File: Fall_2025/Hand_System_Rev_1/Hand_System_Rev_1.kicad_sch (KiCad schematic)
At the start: 33 parts, among them J1 Barrel_Jack, M1 Motor_Servo, M2 Motor_Servo, M3 Motor_Servo, M4 Motor_Servo, M5 Motor_Servo, M6 Motor_Servo, M7 Stepper_Motor, U1 ESP32-DEVKITC-32UE, U2 LM2596, U3 A4988_Stepper_Motor_Driver, U5 MAX9814ETD_T

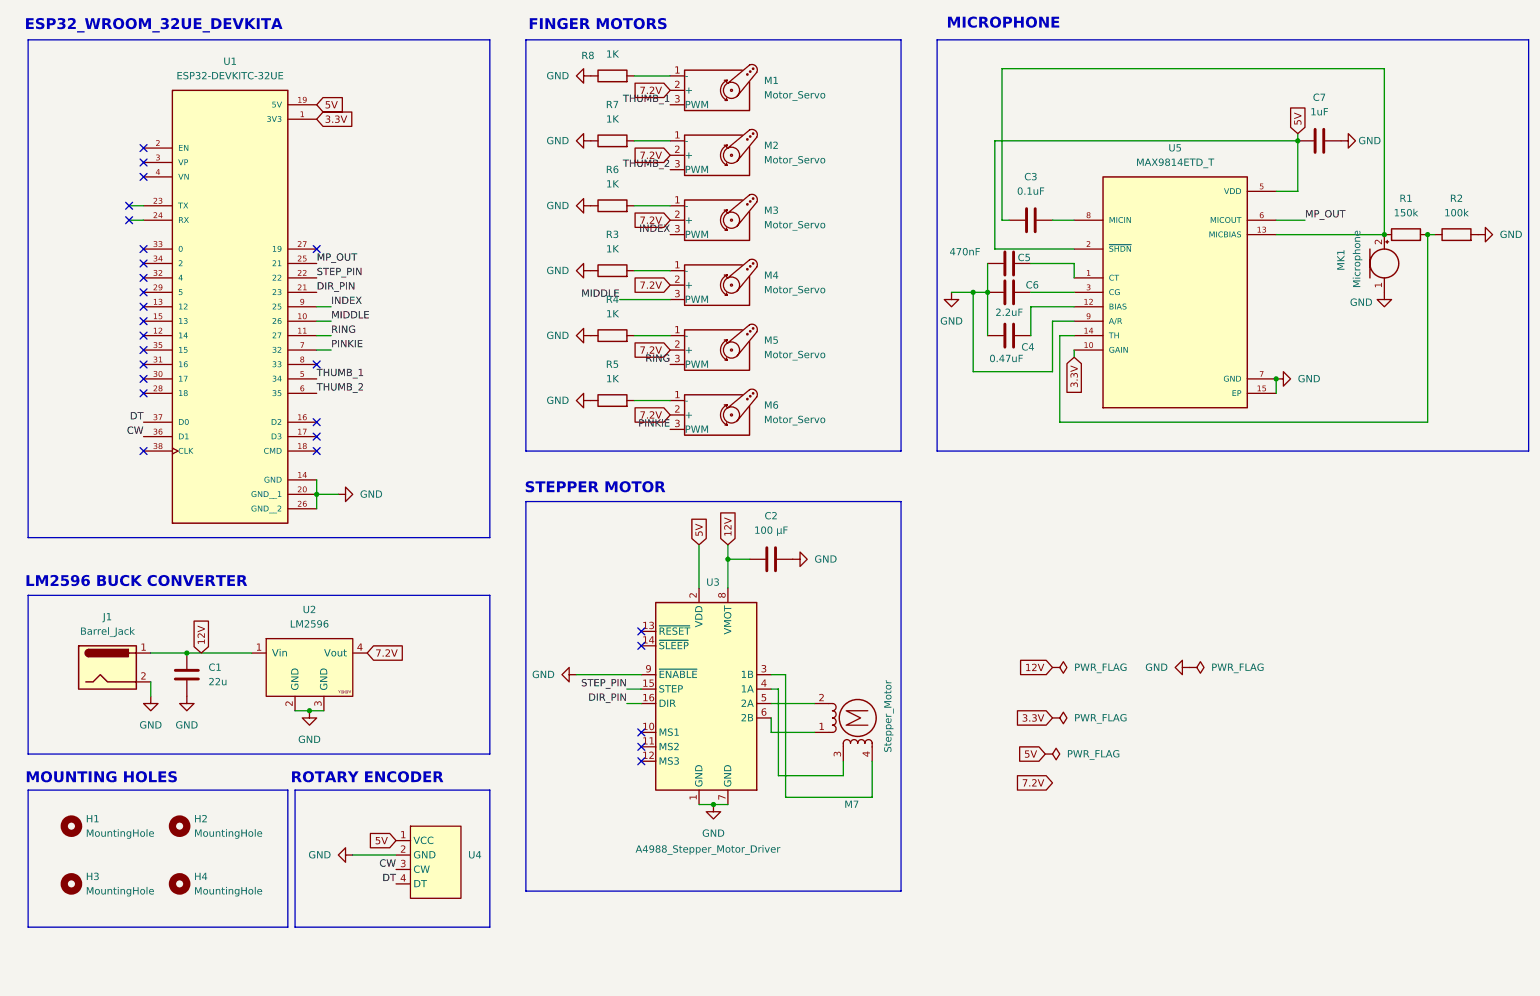
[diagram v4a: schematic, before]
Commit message: update electrical schematic to include 10 servo motors, two buck converteds, and removed microphone
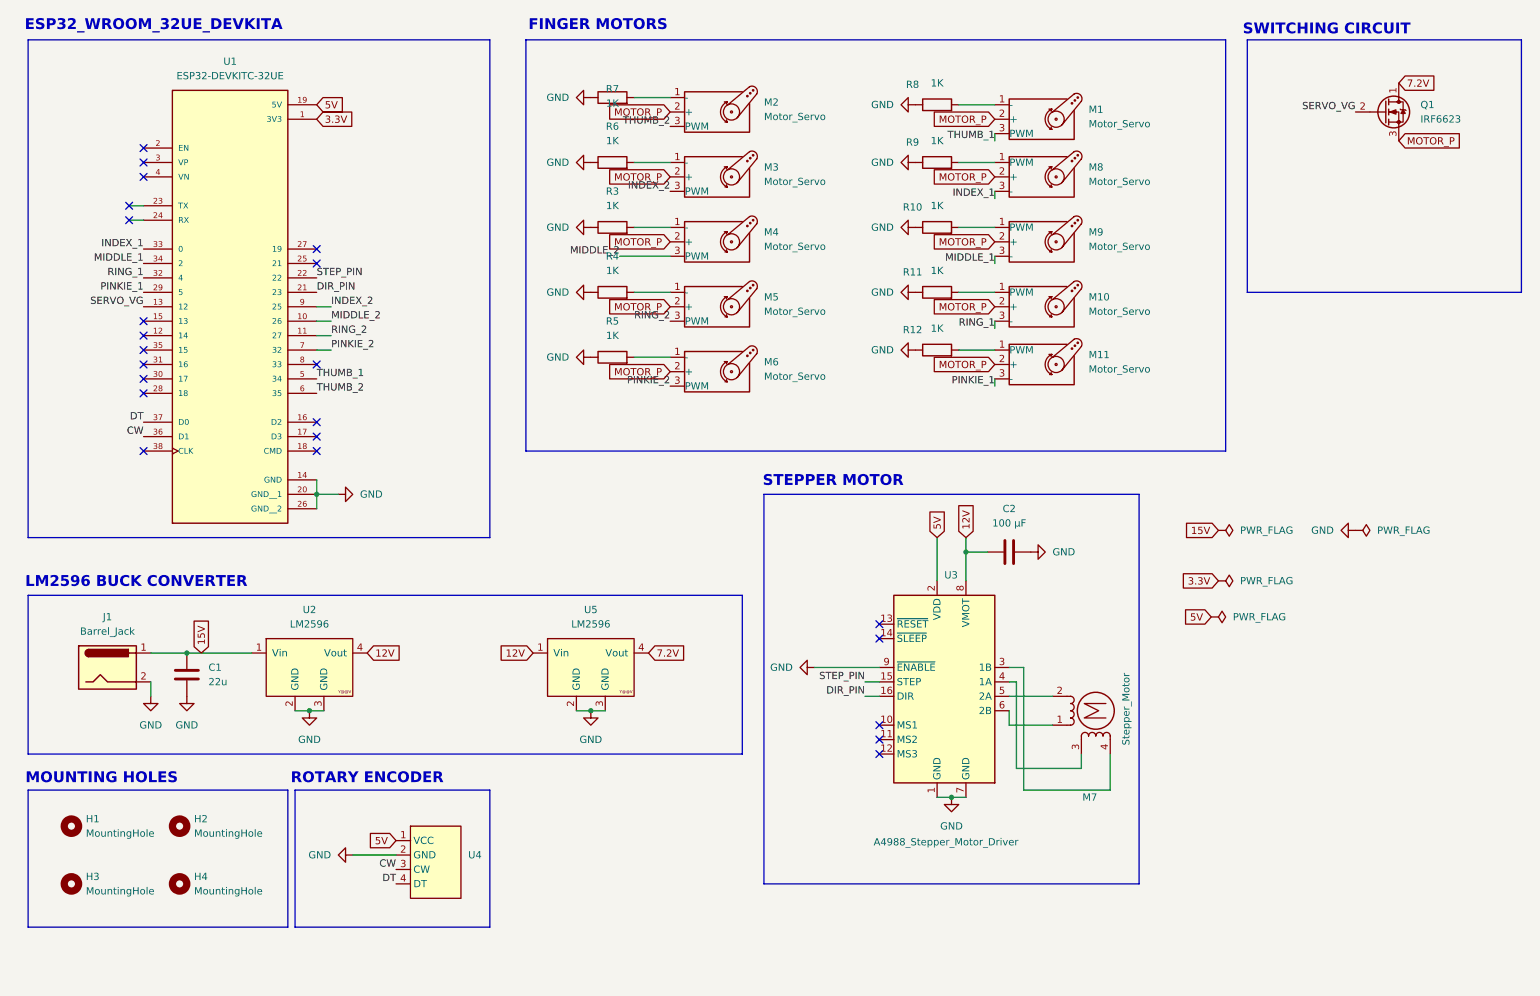
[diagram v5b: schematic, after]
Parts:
- removed C3: 0.1uF, Capacitor_SMD:C_0805_2012Metric, symbol Device:C
- removed C4: 0.47uF, Capacitor_SMD:C_0805_2012Metric, symbol Device:C
- removed C5: 470nF, Capacitor_SMD:C_0805_2012Metric, symbol Device:C
- removed C6: 2.2uF, Capacitor_SMD:C_0805_2012Metric, symbol Device:C
- removed C7: 1uF, Capacitor_SMD:C_0805_2012Metric, symbol Device:C
- removed MK1: Microphone, Sensor_Audio:POM-2244P-C3310-2-R, symbol Device:Microphone
- removed R1: 150k, Resistor_SMD:R_0805_2012Metric, symbol Device:R
- removed R2: 100k, Resistor_SMD:R_0805_2012Metric, symbol Device:R
- removed U5: MAX9814ETD_T, MAX9814ETD_T:SON40P300X300X80-15N, symbol MAX9814ETD_T:MAX9814ETD_T
- added M10, M11, M8, M9: Motor_Servo, symbol Motor:Motor_Servo
- added Q1: IRF6623, Package_DirectFET:DirectFET_ST, symbol Transistor_FET:IRF6623
- added R10, R11, R12, R9: 1K, Resistor_SMD:R_0805_2012Metric, symbol Device:R
- added U5: LM2596, PCB_Components:LM2596, symbol Schematic:LM2596
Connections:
- net 12V: now also U2.4 (Vout), U5.1 (Vin); no longer C1.1, J1.1, U2.1 (Vin)
- net 7.2V: now also Q1.1 (D), U5.4 (Vout); no longer M1.2 (+), M2.2 (+), M3.2 (+), M4.2 (+), M5.2 (+), M6.2 (+), U2.4 (Vout)
- net GND: now also R10.1, R11.1, R12.1, R9.1, U5.2 (GND), U5.3 (GND)
- net SERVO_VG: now reaches U1.13 (12)
- net SERVO_VG: now also Q1.2 (G)
- net PINKIE_1: now reaches U1.29 (5)
- net PINKIE_1: now also M11.3 (-)
- net RING_1: now reaches U1.32 (4)
- net RING_1: now also M10.3 (-)
- net INDEX_1: now reaches U1.33 (0)
- net INDEX_1: now also M8.3 (-)
- net MIDDLE_1: now reaches U1.34 (2)
- net MIDDLE_1: now also M9.3 (-)
- net INDEX renamed INDEX_2
- net MIDDLE renamed MIDDLE_2
- net MP_OUT: no longer names the net of U1.25 (21)
- net PINKIE renamed PINKIE_2
- net RING renamed RING_2
- new net: M8.1 (PWM), R9.2
- new net: M10.1 (PWM), R11.2
- new net: M11.1 (PWM), R12.2
- new net: M9.1 (PWM), R10.2
- new net 15V: C1.1, J1.1, U2.1 (Vin)
- new net MOTOR_P: M1.2 (+), M10.2 (+), M11.2 (+), M2.2 (+), M3.2 (+), M4.2 (+), M5.2 (+), M6.2 (+), M8.2 (+), M9.2 (+), Q1.3 (S)
- no-connect marks 27 -> 23
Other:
- note added: "SWITCHING CIRCUIT"
- note removed: "MICROPHONE"
- moved on the sheet: C2, M1, M2, M3, M4, M5, M6, M7, R3, R4, R5, R6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

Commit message: added more stuff for switching circuitry
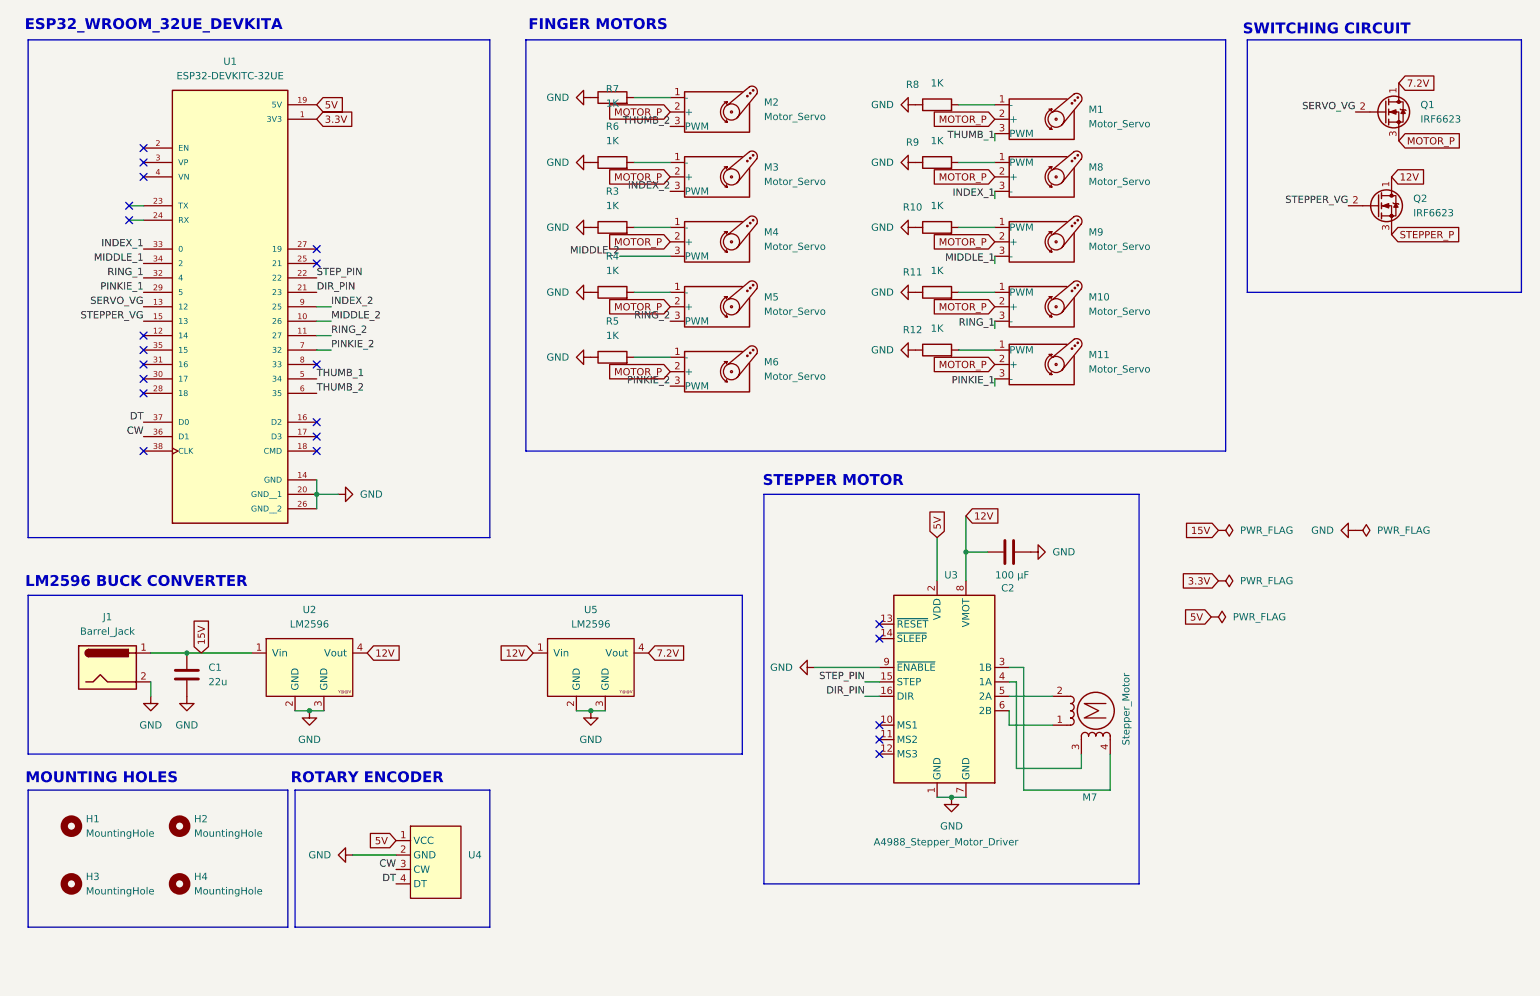
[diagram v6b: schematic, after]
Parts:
- added Q2: IRF6623, Package_DirectFET:DirectFET_ST, symbol Transistor_FET:IRF6623
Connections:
- net 12V: now also Q2.1 (D)
- net STEPPER_VG: now reaches U1.15 (13)
- net STEPPER_VG: now also Q2.2 (G)
- new net STEPPER_P: Q2.3 (S)
- no-connect marks 23 -> 22
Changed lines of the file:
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@@
 	)
 	(no_connect
-		(at 35.56 68.58)
-	)
-	(no_connect
 		(at 35.56 91.44)
 	)
@@
 	(wire
 		(pts
-			(xy 180.34 106.68) (xy 180.34 109.22)
+			(xy 180.34 102.87) (xy 180.34 109.22)
 		)
 		(stroke
@@
 		)
 	)
+	(label "STEPPER_VG"
+		(at 35.56 68.58 180)
+		(effects
+			(font
+				(size 1.27 1.27)
+			)
+			(justify right bottom)
+		)
+	)
 	(label "RING_2"
 		(at 68.58 71.12 0)
@@
 		)
 	)
+	(label "STEPPER_VG"
+		(at 247.65 48.26 180)
+		(effects
+			(font
+				(size 1.27 1.27)
+			)
+			(justify right bottom)
+		)
+	)
 	(global_label "15V"
 		(shape input)
@@
 		)
 	)
+	(global_label "12V"
+		(shape input)
+		(at 180.34 102.87 0)
+		(fields_autoplaced yes)
+		(effects
+			(font
+				(size 1.27 1.27)
+			)
+			(justify left)
+		)
+		(property "Intersheetrefs" "${INTERSHEET_REFS}"
+			(at 186.8328 102.87 0)
+			(effects
+				(font
+					(size 1.27 1.27)
+				)
+				(justify left)
+				(hide yes)
+			)
+		)
+	)
+	(global_label "STEPPER_P"
+		(shape input)
+		(at 255.27 53.34 0)
+		(fields_autoplaced yes)
+		(effects
+			(font
+				(size 1.27 1.27)
+			)
+			(justify left)
+		)
+		(property "Intersheetrefs" "${INTERSHEET_REFS}"
+			(at 268.7779 53.34 0)
+			(effects
+				(font
+					(size 1.27 1.27)
+				)
+				(justify left)
+				(hide yes)
+			)
+		)
+	)
 	(global_label "5V"
 		(shape input)
@@
 		)
 	)
-	(global_label "12V"
+	(global_label "MOTOR_P"
 		(shape input)
-		(at 180.34 106.68 90)
+		(at 128.27 77.47 180)
 		(fields_autoplaced yes)
 		(effects
@@
 				(size 1.27 1.27)
 			)
-			(justify left)
+			(justify right)
 		)
 		(property "Intersheetrefs" "${INTERSHEET_REFS}"
-			(at 180.34 100.1872 90)
+			(at 116.6972 77.47 0)
 			(effects
 				(font
 					(size 1.27 1.27)
 				)
-				(justify left)
+				(justify right)
 				(hide yes)
 			)
@@
 	(global_label "MOTOR_P"
 		(shape input)
-		(at 128.27 77.47 180)
+		(at 185.42 76.2 180)
 		(fields_autoplaced yes)
 		(effects
@@
 		)
 		(property "Intersheetrefs" "${INTERSHEET_REFS}"
-			(at 116.6972 77.47 0)
+			(at 173.8472 76.2 0)
 			(effects
 				(font
@@
 	(global_label "MOTOR_P"
 		(shape input)
-		(at 185.42 76.2 180)
+		(at 128.27 66.04 180)
 		(fields_autoplaced yes)
 		(effects
@@
 		)
 		(property "Intersheetrefs" "${INTERSHEET_REFS}"
-			(at 173.8472 76.2 0)
+			(at 116.6972 66.04 0)
 			(effects
 				(font
@@
 		)
 	)
-	(global_label "MOTOR_P"
+	(global_label "15V"
 		(shape input)
-		(at 128.27 66.04 180)
+		(at 45.72 127 90)
 		(fields_autoplaced yes)
 		(effects
@@
 				(size 1.27 1.27)
 			)
-			(justify right)
+			(justify left)
 		)
 		(property "Intersheetrefs" "${INTERSHEET_REFS}"
-			(at 116.6972 66.04 0)
+			(at 45.72 120.5072 90)
 			(effects
 				(font
 					(size 1.27 1.27)
 				)
-				(justify right)
+				(justify left)
 				(hide yes)
 			)
 		)
 	)
-	(global_label "15V"
+	(global_label "12V"
 		(shape input)
-		(at 45.72 127 90)
+		(at 255.27 43.18 0)
 		(fields_autoplaced yes)
 		(effects
@@
 		)
 		(property "Intersheetrefs" "${INTERSHEET_REFS}"
-			(at 45.72 120.5072 90)
+			(at 261.7628 43.18 0)
 			(effects
 				(font
@@
 		(on_board yes)
 		(dnp no)
-		(fields_autoplaced yes)
 		(property "Reference" "C2"
-			(at 187.96 101.6 90)
+			(at 187.706 115.57 90)
 			(effects
 				(font
@@
 		)
 		(property "Value" "100 μF"
-			(at 187.96 104.14 90)
+			(at 188.468 113.284 90)
 			(effects
 				(font
@@
 					(unit 1)
 				)
+			)
+		)
+	)
+	(symbol
+		(lib_id "Transistor_FET:IRF6623")
+		(at 252.73 48.26 0)
+		(unit 1)
+		(exclude_from_sim no)
+		(in_bom yes)
+		(on_board yes)
+		(dnp no)
+		(fields_autoplaced yes)
+		(property "Reference" "Q2"
+			(at 259.08 46.9899 0)
+			(effects
+				(font
+					(size 1.27 1.27)
+				)
+				(justify left)
+			)
+		)
+		(property "Value" "IRF6623"
+			(at 259.08 49.5299 0)
+			(effects
+				(font
+					(size 1.27 1.27)
+				)
+				(justify left)
+			)
+		)
+		(property "Footprint" "Package_DirectFET:DirectFET_ST"
+			(at 257.81 50.165 0)
+			(effects
+				(font
+					(size 1.27 1.27)
+					(italic yes)
+				)
+				(justify left)
+				(hide yes)
+			)
+		)
+		(property "Datasheet" "https://www.infineon.com/dgdl/irf6623pbf.pdf?fileId=5546d462533600a4015355e8aa811a2d"
+			(at 257.81 52.07 0)
+			(effects
+				(font
+					(size 1.27 1.27)
+				)
+				(justify left)
+				(hide yes)
+			)
+		)
+		(property "Description" "55A Id, 20V Vds, 5.7mOhm Rds, N-Channel MOSFET, DirectFET ST"
+			(at 252.73 48.26 0)
+			(effects
+				(font
+					(size 1.27 1.27)
+				)
+				(hide yes)
+			)
+		)
+		(pin "2"
+		)
+		(pin "1"
+		)
+		(pin "3"
+		)
+		(instances
+			(project "Hand_System_Rev_1"
+				(path "/561f6b17-6c60-4192-990d-3a71dfc69574"
+					(reference "Q2")
+					(unit 1)
+				)

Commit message: added more stuff
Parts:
- added R1, R14: 10k, Resistor_SMD:R_0805_2012Metric, symbol Device:R
- added R13, R15, R16, R2: 1k, Resistor_SMD:R_0805_2012Metric, symbol Device:R
- M10, M11, M8, M9: footprint (none) -> Connector_PinHeader_2.54mm:PinHeader_1x03_P2.54mm_Vertical
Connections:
- net 12V: now also R14.2; no longer C2.1, Q2.1 (D), U3.8 (VMOT)
- net 7.2V: now also R1.1; no longer Q1.1 (D)
- net CW: now also U1.13 (12); no longer U1.36 (D1)
- net DT: now also U1.12 (14); no longer U1.37 (D0)
- net INDEX_1: now also U1.25 (21); no longer U1.33 (0)
- net INDEX_2: now also U1.27 (19); no longer U1.9 (25)
- net MIDDLE_1: now also U1.28 (18); no longer U1.34 (2)
- net MIDDLE_2: now also U1.29 (5); no longer U1.10 (26)
- net MOTOR_P: now also R13.2; no longer Q1.3 (S)
- net PINKIE_1: now also U1.32 (4); no longer U1.29 (5)
- net PINKIE_2: now also U1.33 (0); no longer U1.7 (32)
- net RING_1: now also U1.30 (17); no longer U1.32 (4)
- net RING_2: now also U1.31 (16); no longer U1.11 (27)
- net SERVO_VG: now also U1.16 (D2), R2.1; no longer Q1.2 (G), U1.13 (12)
- net THUMB_1: now also U1.23 (TX); no longer U1.5 (34)
- net THUMB_2: now also U1.24 (RX); no longer U1.6 (35)
- net STEPPER_P: no longer names the net of Q2.3 (S)
- net STEPPER_P: now also R16.1
- net STEPPER_VG: no longer names the net of Q2.2 (G)
- net STEPPER_VG: now also R15.2; no longer U1.15 (13)
- new net: Q1.3 (S), R13.1
- new net: Q2.1 (D), R14.1
- new net: Q1.1 (D), R1.2
- new net: Q1.2 (G), R2.2
- new net STP_P: C2.1, R16.2, U3.8 (VMOT)
- new net STP_VG: R15.1, U1.15 (13)
- no-connect marks 22 -> 13
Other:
- moved on the sheet: Q1, Q2
